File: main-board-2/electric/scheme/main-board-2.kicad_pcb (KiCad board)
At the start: 2 copper layers, 85 x 56 mm, 120 parts, among them K1 power-switch, K2 usb-power-switch, P1 batt, P10 screw-3, P11 screw-1, P12 screw-4, P13 screw-2, P14 gpio-big, P15 gpio-small, P16 moto-1, P17 moto-2, P3 trigger-btn, P4 CONN_3X2, P5 reg-short-to-gnd-1, P6 reg-short-to-gnd-2, P7 bootloader, P8 cross board conn, P9 rst, Q1 IRLML2244, Q10 IRLML2244, Q11 sot223, Q12 bc857, Q13 irlml2244, Q2 BC847, Q3 IRLML2244, Q4 IRLML2244, Q5 BC847, Q6 BC847, Q7 BC847, Q8 BC847, Q9 IRLML2244, U5 LM293, U6 L298, U7 MINI-USB-B, X1 8MHz

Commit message: Placing elements...
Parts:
- added P2: CONN_4, PIN_ARRAY_4x1, F.Cu at (153.5, 200.5)
- added R49: 30k, SM0805, F.Cu at (325.1, 179.1)
- added U1: LM317AEMP, SOT223, B.Cu at (187.5, 148.5)
- added U2: LM317AT, my_TO220, B.Cu at (187.5, 143.3)
- added U3: LM317AEMP, SOT223, B.Cu at (175.6, 143.2)
- added U4: LM317AT, my_TO220, B.Cu at (180.8, 143.2)
- C15, C16, D4, D8, P5, P6, Q3, Q4, Q5, Q6, R18, R19, R2, R20, R22, R24, W2, W3: moved to B.Cu
- C5: value 54u -> 4u7; footprint C2V10 -> SM0805
- C6: value 4u7 -> 54u; footprint SM0805 -> C2V10
- R10, R27, R41: value 30k -> 1k
- R12: value 50 -> 30k
- R13: value 30k -> 50
- R14: value 10k -> 30k
- R17: value 30k -> 10k
- R21: value 1k -> 30k; moved to B.Cu
- R23: value 30k -> 1k; moved to B.Cu
- R25, R40, R42, R9: value 1k -> 30k
- R31: value 22 -> 30k
- R33: value 1k5 -> 22
- R34: value 100k -> 1k5
- R35: value 0.1 -> 100k
- R39: value 30k -> 0.1
- R45: value 9 -> 1k
- R46: value 9 -> 3
- R47: value 30k -> 3
- R7: value 3k -> 30k
- R8: value 30k -> 3k
- moved C6 198.5 mm to (109.5, 50.3)
- moved P6 187.3 mm to (180.8, 138.6)
- moved C3 180.4 mm to (188.7, 146.1), turned to 270 degrees
- moved Q2 150.7 mm to (163.7, 91.4), turned to 270 degrees
- moved W1 150.4 mm to (158.8, 90.3), turned to 180 degrees
- moved R7 145.8 mm to (161.5, 93.1), turned to 180 degrees
- moved W6 142.2 mm to (286.9, 74.5), turned to 180 degrees
- moved C5 134.0 mm to (190.5, 146.1), turned to 270 degrees
- moved R42 129.9 mm to (293.1, 79.5)
- moved R10 127.9 mm to (167.1, 92.5), turned to 180 degrees
- moved Q1 126.8 mm to (158.4, 92.1), turned to 270 degrees
- moved R9 125.7 mm to (162.2, 89.2), turned to 90 degrees
- moved R45 124.9 mm to (287.0, 88.4)
- moved R38 124.5 mm to (282.7, 77.9)
- moved R39 124.0 mm to (287.0, 75.9), turned to 180 degrees
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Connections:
- C4 pad 1: VDD -> N-0000082
- C5 pad 1: N-0000083 -> VDD
- C6 pad 1: /+5V -> N-0000082
- C9 pad 2: N-0000058 -> N-0000055
- K1 pad 1: N-0000083 -> N-0000082
- K2 pad 3: N-0000030 -> N-0000032
- P7 pad 2: N-0000060 -> N-0000061
- P8 pad 1: N-0000078 -> N-0000079
- P9 pad 1: N-0000058 -> N-0000055
- Q1 pad G: N-000005 -> N-000006
- Q10 pad G: N-0000046 -> N-0000010
- Q11 pad G: N-0000027 -> N-0000031
- Q12 pad 1: N-0000030 -> N-0000032
- Q12 pad 2: N-0000011 -> N-0000016
- Q12 pad 3: N-000007 -> N-000008
- Q13 pad G: N-000007 -> N-000008
- Q13 pad S: N-0000011 -> N-0000016
- Q2 pad 2: N-000002 (its old number) -> N-000005
- Q2 pad 3: N-000005 -> N-000004
- Q3 pad G: N-000009 -> N-0000014
- Q4 pad G: N-0000028 -> N-0000012
- Q5 pad 2: N-0000065 -> N-0000066
- Q5 pad 3: N-0000010 -> N-000009
- Q6 pad 2: N-0000079 -> N-0000084
- Q6 pad 3: N-000008 -> N-0000013
- Q7 pad 1: N-0000026 -> N-0000029
- Q7 pad 2: N-0000025 -> N-0000030
- Q7 pad 3: N-0000027 -> N-0000031
- Q8 pad 3: N-0000045 -> N-0000011
- Q9 pad G: N-0000027 -> N-0000031
- R10 pad 1: GND -> /rpi-pwr-en
- R10 pad 2: /rpi-pwr-en -> N-000005
- R11 pad 1: N-0000060 -> GND
- R11 pad 2: GND -> /rpi-pwr-en
- R12 pad 1: N-0000071 -> N-0000061
- R12 pad 2: N-0000069 -> GND
- R13 pad 1: VDD -> N-0000071
- R13 pad 2: N-0000058 -> N-0000069
- R14 pad 1: /addon-vdd -> VDD
- R14 pad 2: /sda-int -> N-0000055
- R15 pad 2: /scl-int -> /sda-int
- R16 pad 1: N-0000078 -> /addon-vdd
- R16 pad 2: /addon-trigger -> /scl-int
- R17 pad 1: N-0000010 -> N-0000079
- R17 pad 2: N-000009 -> /addon-trigger
- R18 pad 1: N-000008 -> N-000009
- R18 pad 2: N-0000028 -> N-0000014
- R19 pad 1: N-0000010 -> N-0000013
- R19 pad 2: /+5V -> N-0000012
- R20 pad 1: N-000008 -> N-000009
- R20 pad 2: VDD -> /+5V
- R21 pad 1: /addon-pwr-en -> N-0000013
- R21 pad 2: N-0000065 -> VDD
- R22 pad 2: N-0000079 -> N-0000066
- R23 pad 1: GND -> /addon-pwr-en
- R23 pad 2: /addon-pwr-en -> N-0000084
- R24 pad 2: /moto-en -> /addon-pwr-en
- R25 pad 1: /moto-en -> GND
- R25 pad 2: N-0000025 -> /moto-en
- R26 pad 2: N-0000067 -> N-0000030
- R27 pad 1: /batt+ -> /moto-en
- R27 pad 2: N-0000027 -> N-0000067
- R28 pad 1: N-0000026 -> /batt+
- R28 pad 2: GND -> N-0000031
- R29 pad 1: /+5V -> N-0000029
- R29 pad 2: N-0000045 -> GND
- R30 pad 1: N-0000045 -> /+5V
- R30 pad 2: N-0000046 -> N-0000011
- R31 pad 1: /d- -> N-0000011
- R31 pad 2: N-0000055 -> N-0000010
- R32 pad 1: /d+ -> /d-
- R32 pad 2: N-0000091 -> N-0000051
- R33 pad 1: N-0000091 -> /d+
- R33 pad 2: /usb-connected -> N-0000092
- R34 pad 1: GND -> N-0000092
- R34 pad 2: N-0000056 -> /usb-connected
- R35 pad 1: /cur-sense-2 -> GND
- R35 pad 2: GND -> N-0000052
- R36 pad 1: /cur-sense-1 -> /cur-sense-2
- R37 pad 1: /cur-sense-2 -> /cur-sense-1
- R38 pad 1: /cur-sense-1 -> /cur-sense-2
- R39 pad 1: VDD -> /cur-sense-1
- R39 pad 2: N-0000048 -> GND
- R40 pad 1: N-0000048 -> VDD
- R40 pad 2: GND -> N-0000044
- R41 pad 1: VDD -> N-0000044
- R41 pad 2: N-0000043 (its old number) -> GND
- R42 pad 1: N-0000043 (its old number) -> VDD
- R42 pad 2: GND -> N-0000042
- R43 pad 1: /moto-en -> N-0000042
- R43 pad 2: /moto-en-2 -> GND
- R44 pad 2: /moto-en-1 -> /moto-en-2
- R45 pad 1: N-0000030 -> /moto-en
- R45 pad 2: N-0000011 -> /moto-en-1
- R46 pad 1: N-0000030 -> N-0000032
- R46 pad 2: N-0000011 -> N-0000016
- R47 pad 1: GND -> N-0000032
- R47 pad 2: N-000007 -> N-0000016
- R48 pad 1: N-000007 -> GND
- R48 pad 2: /batt+ -> N-000008
- R6 pad 1: N-0000084 -> N-0000083
- R7 pad 1: N-0000084 -> N-000004
- R7 pad 2: N-0000083 -> N-000006
- R8 pad 1: N-000005 -> N-0000083
- R8 pad 2: /+5V -> N-0000082
- R9 pad 1: /rpi-pwr-en -> N-000004
- R9 pad 2: N-000002 (its old number) -> /+5V
- U5 pad 3: N-0000048 -> N-0000044
- U5 pad 5: N-0000043 (its old number) -> N-0000042
- U7 pad 2: N-0000055 -> N-0000051
- U7 pad 3: N-0000091 -> N-0000092
- U7 pad 4: N-0000056 -> N-0000052
- W10 pad 1: N-0000030 -> N-0000032
- stm1 pad 44: N-0000060 -> N-0000061
- stm1 pad 7: N-0000058 -> N-0000055

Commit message: a
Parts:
- moved C6 124.4 mm to (177.8, 154.3), turned to 90 degrees
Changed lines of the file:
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@@
   )
   (module C2V10 (layer F.Cu)
-    (at 109.474 50.292)
+    (at 177.8 154.305 90)
     (descr "Condensateur polarise")
     (tags CP)
-    (fp_text reference C6 (at 0 2.54) (layer F.SilkS)
+    (fp_text reference C6 (at 0 2.54 90) (layer F.SilkS)
       (effects (font (size 1.27 1.27) (thickness 0.254)))
     )
-    (fp_text value 54u (at 0 -2.54) (layer F.SilkS)
+    (fp_text value 54u (at 0 -2.54 90) (layer F.SilkS)
       (effects (font (size 1.27 1.27) (thickness 0.254)))
     )
     (fp_circle (center 0 0) (end 4.826 -2.794) (layer F.SilkS) (width 0.3048))
-    (pad 1 thru_hole rect (at -2.54 0) (size 1.778 1.778) (drill 1.016)
+    (pad 1 thru_hole rect (at -2.54 0 90) (size 1.778 1.778) (drill 1.016)
       (layers *.Cu *.Mask F.SilkS)
       (net 77 N-0000082)
     )
-    (pad 2 thru_hole circle (at 2.54 0) (size 1.778 1.778) (drill 1.016)
+    (pad 2 thru_hole circle (at 2.54 0 90) (size 1.778 1.778) (drill 1.016)
       (layers *.Cu *.Mask F.SilkS)
       (net 45 GND)

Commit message: a
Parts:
- moved Q12 167.6 mm to (156.5, 162.4)
- moved R48 167.6 mm to (159.4, 166.1)
- moved R49 167.6 mm to (157.9, 168.9)
- moved Q13 167.6 mm to (156.7, 166.1)
- moved R46 167.6 mm to (153.9, 162.4)
- moved R47 167.6 mm to (152.1, 162.4)
- moved W10 167.6 mm to (153.0, 166.0)
- moved R11 59.5 mm to (151.4, 147.8), turned to 270 degrees
- moved R10 58.1 mm to (149.6, 147.8), turned to 90 degrees
- moved Q2 54.8 mm to (150.5, 144.7), turned to 180 degrees
- moved R9 53.3 mm to (151.3, 141.4)
- moved R7 50.5 mm to (148.6, 141.9)
- moved W1 49.0 mm to (148.8, 138.3)
- moved Q1 48.2 mm to (148.6, 139.3), turned to 180 degrees
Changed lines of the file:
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@@
   )
   (module SOT23GDS (layer F.Cu)
-    (at 158.369 92.075 270)
+    (at 148.59 139.319 180)
     (descr "Module CMS SOT23 Transistore EBC")
     (tags "CMS SOT")
     (attr smd)
-    (fp_text reference Q1 (at 0 -2.159 270) (layer F.SilkS)
+    (fp_text reference Q1 (at 0 -2.159 180) (layer F.SilkS)
       (effects (font (size 0.762 0.762) (thickness 0.12954)))
     )
-    (fp_text value IRLML2244 (at 0 0 270) (layer F.SilkS)
+    (fp_text value IRLML2244 (at 0 0 180) (layer F.SilkS)
       (effects (font (size 0.762 0.762) (thickness 0.12954)))
     )
@@
     (fp_line (start 1.524 0.381) (end -1.524 0.381) (layer F.SilkS) (width 0.11938))
     (fp_line (start -1.524 0.381) (end -1.524 -0.381) (layer F.SilkS) (width 0.11938))
-    (pad S smd rect (at -0.889 -1.016 270) (size 0.9144 0.9144)
+    (pad S smd rect (at -0.889 -1.016 180) (size 0.9144 0.9144)
       (layers F.Cu F.Paste F.Mask)
       (net 1 /+5V)
     )
-    (pad G smd rect (at 0.889 -1.016 270) (size 0.9144 0.9144)
+    (pad G smd rect (at 0.889 -1.016 180) (size 0.9144 0.9144)
       (layers F.Cu F.Paste F.Mask)
       (net 66 N-000006)
     )
-    (pad D smd rect (at 0 1.016 270) (size 0.9144 0.9144)
+    (pad D smd rect (at 0 1.016 180) (size 0.9144 0.9144)
       (layers F.Cu F.Paste F.Mask)
       (net 52 N-000002)
@@
   )
   (module SOT23GDS (layer F.Cu)
-    (at 323.977 176.276)
+    (at 156.718 166.116)
     (descr "Module CMS SOT23 Transistore EBC")
     (tags "CMS SOT")
@@
   )
   (module SOT23EBC (layer F.Cu)
-    (at 323.723 172.593 90)
+    (at 156.464 162.433 90)
     (descr "Module CMS SOT23 Transistore EBC")
     (tags "CMS SOT")
@@
   )
   (module SOT23EBC (layer F.Cu)
-    (at 163.703 91.44 270)
+    (at 150.495 144.653 180)
     (descr "Module CMS SOT23 Transistore EBC")
     (tags "CMS SOT")
     (attr smd)
-    (fp_text reference Q2 (at 0 -2.413 270) (layer F.SilkS)
+    (fp_text reference Q2 (at 0 -2.413 180) (layer F.SilkS)
       (effects (font (size 0.762 0.762) (thickness 0.2032)))
     )
-    (fp_text value BC847 (at 0 0 270) (layer F.SilkS) hide
+    (fp_text value BC847 (at 0 0 180) (layer F.SilkS) hide
       (effects (font (size 0.762 0.762) (thickness 0.2032)))
     )
@@
     (fp_line (start 1.524 0.381) (end -1.524 0.381) (layer F.SilkS) (width 0.127))
     (fp_line (start -1.524 0.381) (end -1.524 -0.381) (layer F.SilkS) (width 0.127))
-    (pad 1 smd rect (at -0.889 -1.016 270) (size 0.9144 0.9144)
+    (pad 1 smd rect (at -0.889 -1.016 180) (size 0.9144 0.9144)
       (layers F.Cu F.Paste F.Mask)
       (net 45 GND)
     )
-    (pad 2 smd rect (at 0.889 -1.016 270) (size 0.9144 0.9144)
+    (pad 2 smd rect (at 0.889 -1.016 180) (size 0.9144 0.9144)
       (layers F.Cu F.Paste F.Mask)
       (net 62 N-000005)
     )
-    (pad 3 smd rect (at 0 1.016 270) (size 0.9144 0.9144)
+    (pad 3 smd rect (at 0 1.016 180) (size 0.9144 0.9144)
       (layers F.Cu F.Paste F.Mask)
       (net 58 N-000004)
@@
   )
   (module SM0805 (layer F.Cu)
-    (at 161.544 93.091 180)
+    (at 148.59 141.859 180)
     (attr smd)
     (fp_text reference R7 (at 0 -0.3175 180) (layer F.SilkS)
@@
   )
   (module SM0805 (layer F.Cu)
-    (at 321.183 172.593 90)
+    (at 153.924 162.433 90)
     (attr smd)
     (fp_text reference R46 (at 0 -0.3175 90) (layer F.SilkS)
@@
   )
   (module SM0805 (layer F.Cu)
-    (at 162.179 89.154 90)
+    (at 151.257 141.351 90)
     (attr smd)
     (fp_text reference R9 (at 0 -0.3175 90) (layer F.SilkS)
@@
   )
   (module SM0805 (layer F.Cu)
-    (at 167.132 92.456 180)
+    (at 149.606 147.828 90)
     (attr smd)
-    (fp_text reference R10 (at 0 -0.3175 180) (layer F.SilkS)
+    (fp_text reference R10 (at 0 -0.3175 90) (layer F.SilkS)
       (effects (font (size 0.50038 0.50038) (thickness 0.10922)))
     )
-    (fp_text value 1k (at 0 0.381 180) (layer F.SilkS)
+    (fp_text value 1k (at 0 0.381 90) (layer F.SilkS)
       (effects (font (size 0.50038 0.50038) (thickness 0.10922)))
     )
@@
     (fp_line (start 1.524 -0.762) (end 1.524 0.762) (layer F.SilkS) (width 0.09906))
     (fp_line (start 1.524 0.762) (end 0.508 0.762) (layer F.SilkS) (width 0.09906))
-    (pad 1 smd rect (at -0.9525 0 180) (size 0.889 1.397)
+    (pad 1 smd rect (at -0.9525 0 90) (size 0.889 1.397)
       (layers F.Cu F.Paste F.Mask)
       (net 33 /rpi-pwr-en)
     )
-    (pad 2 smd rect (at 0.9525 0 180) (size 0.889 1.397)
+    (pad 2 smd rect (at 0.9525 0 90) (size 0.889 1.397)
       (layers F.Cu F.Paste F.Mask)
       (net 62 N-000005)
@@
   )
   (module SM0805 (layer F.Cu)
-    (at 167.132 90.424)
+    (at 151.384 147.828 270)
     (attr smd)
-    (fp_text reference R11 (at 0 -0.3175) (layer F.SilkS)
+    (fp_text reference R11 (at 0 -0.3175 270) (layer F.SilkS)
       (effects (font (size 0.50038 0.50038) (thickness 0.10922)))
     )
-    (fp_text value 30k (at 0 0.381) (layer F.SilkS)
+    (fp_text value 30k (at 0 0.381 270) (layer F.SilkS)
       (effects (font (size 0.50038 0.50038) (thickness 0.10922)))
     )
@@
     (fp_line (start 1.524 -0.762) (end 1.524 0.762) (layer F.SilkS) (width 0.09906))
     (fp_line (start 1.524 0.762) (end 0.508 0.762) (layer F.SilkS) (width 0.09906))
-    (pad 1 smd rect (at -0.9525 0) (size 0.889 1.397)
+    (pad 1 smd rect (at -0.9525 0 270) (size 0.889 1.397)
       (layers F.Cu F.Paste F.Mask)
       (net 45 GND)
     )
-    (pad 2 smd rect (at 0.9525 0) (size 0.889 1.397)
+    (pad 2 smd rect (at 0.9525 0 270) (size 0.889 1.397)
       (layers F.Cu F.Paste F.Mask)
       (net 33 /rpi-pwr-en)
@@
   )
   (module SM0805 (layer F.Cu)
-    (at 326.644 176.276 270)
+    (at 159.385 166.116 270)
     (attr smd)
     (fp_text reference R48 (at 0 -0.3175 270) (layer F.SilkS)
@@
   )
   (module SM0805 (layer F.Cu)
-    (at 319.405 172.593 90)
+    (at 152.146 162.433 90)
     (attr smd)
     (fp_text reference R47 (at 0 -0.3175 90) (layer F.SilkS)
@@
   )
   (module PIN_ARRAY_2X1 (layer F.Cu)
-    (at 320.294 176.149 270)
+    (at 153.035 165.989 270)
     (descr "Connecteurs 2 pins")
     (tags "CONN DEV")
@@
   )
   (module PIN_ARRAY_2X1 (layer F.Cu)
-    (at 158.75 90.297 180)
+    (at 148.844 138.303 180)
     (descr "Connecteurs 2 pins")
     (tags "CONN DEV")
@@
   )
   (module SM0805 (layer F.Cu)
-    (at 325.12 179.07 180)
+    (at 157.861 168.91 180)
     (attr smd)
     (fp_text reference R49 (at 0 -0.3175 180) (layer F.SilkS)

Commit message: Placing components...
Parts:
- Q10, Q11, Q7, Q8, Q9, R25, R26, R27, R28, R29, R30, R31: moved to B.Cu
- moved R42 145.5 mm to (212.1, 200.4), turned to 90 degrees
- moved R43 139.0 mm to (214.9, 199.4), turned to 0 degrees
- moved R45 138.8 mm to (214.9, 207.0), turned to 180 degrees
- moved R36 137.2 mm to (214.1, 194.9)
- moved R37 137.2 mm to (218.4, 196.7)
- moved R38 137.2 mm to (214.1, 196.7)
- moved R39 137.2 mm to (218.4, 194.8)
- moved U5 137.2 mm to (216.5, 203.2)
- moved W8 137.2 mm to (219.2, 211.1)
- moved W9 137.2 mm to (214.4, 211.1)
- moved W6 137.2 mm to (218.3, 193.4)
- moved W7 137.2 mm to (214.1, 193.4)
- moved R40 137.1 mm to (221.0, 200.4), turned to 90 degrees
- moved R41 135.6 mm to (218.2, 199.4), turned to 180 degrees
- moved R44 135.4 mm to (218.3, 207.0), turned to 0 degrees
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
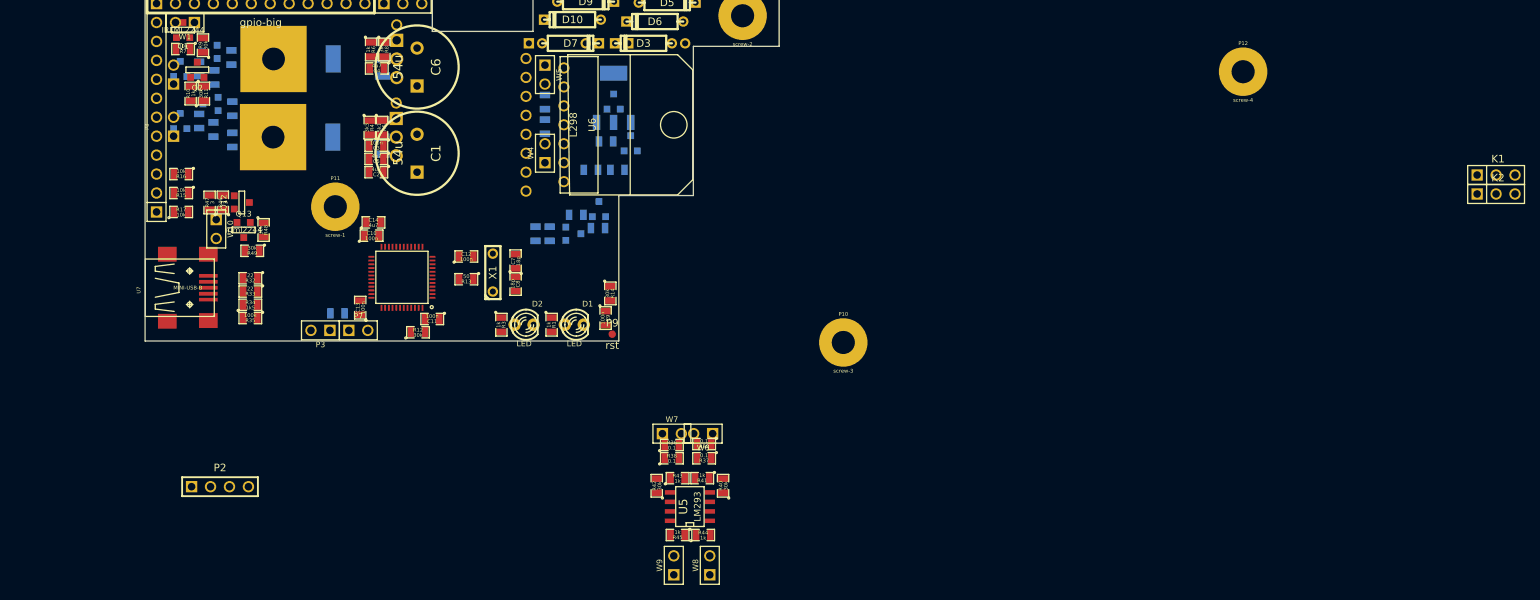
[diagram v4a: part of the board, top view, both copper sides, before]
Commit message: Placing components.
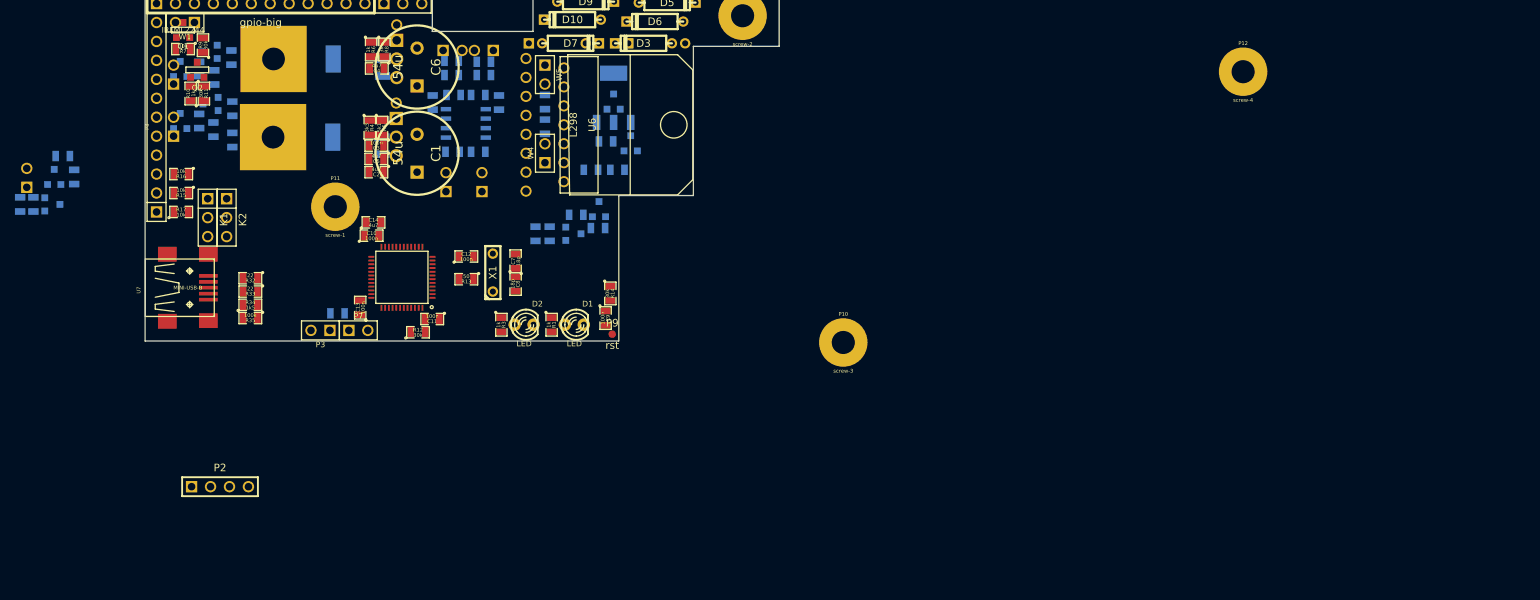
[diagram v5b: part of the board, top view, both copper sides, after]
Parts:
- Q12, Q13, R36, R37, R38, R39, R40, R41, R42, R43, R44, R45, R46, R47, R48, R49, U5, W10, W6, W7, W8, W9: moved to B.Cu
- moved K1 172.8 mm to (151.9, 164.5), turned to 270 degrees
- moved K2 170.2 mm to (154.4, 164.5), turned to 270 degrees
- moved R40 64.5 mm to (182.1, 149.0)
- moved W8 62.4 mm to (183.8, 159.7)
- moved R37 61.5 mm to (184.6, 145.4), turned to 0 degrees
- moved R39 61.5 mm to (184.6, 143.4), turned to 0 degrees
- moved R44 61.4 mm to (184.7, 155.6), turned to 180 degrees
- moved W6 61.4 mm to (184.7, 142.0), turned to 0 degrees
- moved R41 61.2 mm to (184.8, 148.0), turned to 0 degrees
- moved U5 59.5 mm to (186.5, 151.8)
- moved R43 57.9 mm to (188.2, 148.0), turned to 180 degrees
- moved R45 57.9 mm to (188.2, 155.6), turned to 0 degrees
- moved W9 57.4 mm to (188.7, 159.7)
- moved R38 57.2 mm to (188.9, 145.4), turned to 180 degrees
- moved R36 57.2 mm to (188.9, 143.6), turned to 180 degrees
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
